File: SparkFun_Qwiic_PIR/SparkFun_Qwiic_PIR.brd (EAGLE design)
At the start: 38.1 x 25.5 mm, 39 parts, among them J1 QWIIC_RIGHT_ANGLE, J2 QWIIC_RIGHT_ANGLE, Q1 220mA/50V/3.5Ω, Q2 220mA/50V/3.5Ω, U1 PL-N823-01PL-N823-01_LENS, U2 ADS1015, U3 TPS61200

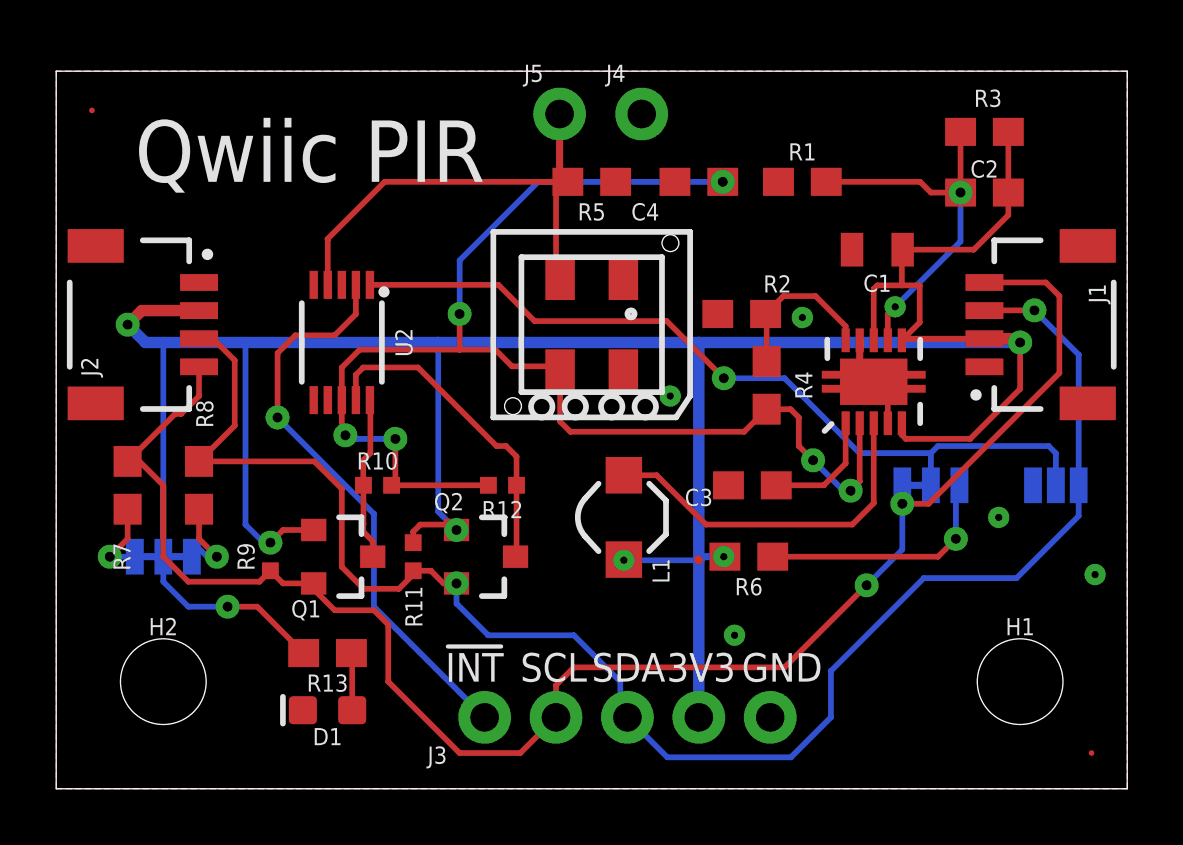
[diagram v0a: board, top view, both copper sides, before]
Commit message: Upload 15V revision with LTC3122 Boost IC
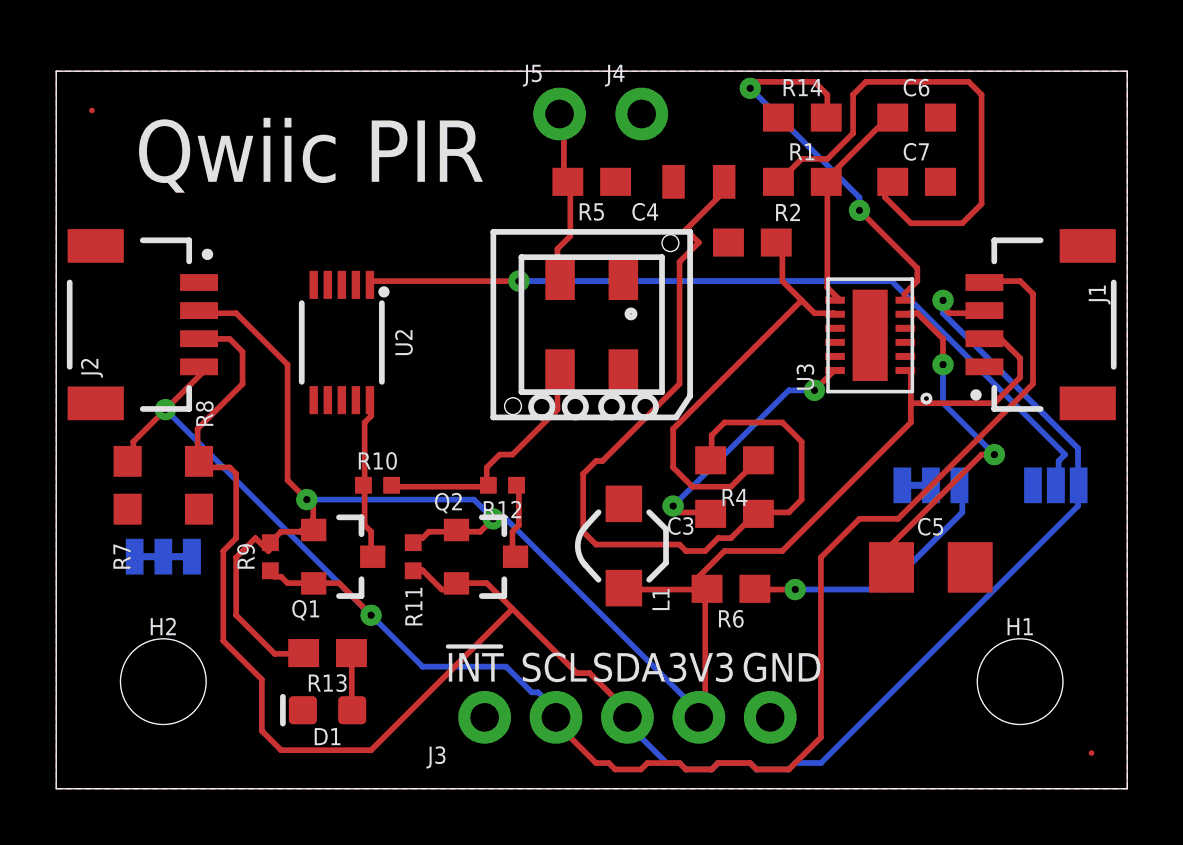
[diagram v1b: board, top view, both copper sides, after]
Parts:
- removed C1: 10uF, SparkFun-Capacitors:0805
- removed C2: 1.0uF, SparkFun-Capacitors:0603
- removed R3: 2.0M, SparkFun-Resistors:0603
- added C5: 4.7uF, SparkFun-Capacitors:1206
- added C6, C7: 1nF, SparkFun-Capacitors:0603
- added R14: 0.27, SparkFun-Resistors:0603
- C3: value 1.0uF -> 0.1uF
- C4: device SparkFun-Capacitors:0603 -> SparkFun-Capacitors:0805
- R2: value 200k -> 330
- R4: value 2.0M -> 3.3k
- U3: value TPS61200 -> LTC3122; device SparkFun-IC-Power:QFN-10_PAD -> LTC3122:LTC3122EDE#PBF
- moved R4 2.90 mm to (24.1, 11.7), turned to 180 degrees
- moved R2 2.57 mm to (24.8, 19.4)
- moved U3 1.66 mm to (29.0, 16.1), turned to 90 degrees
- moved R6 1.31 mm to (24.0, 7.11)
- moved C3 1.20 mm to (24.1, 9.78)
- moved L1 1.02 mm to (20.2, 8.64)
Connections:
- new net N$10: R2.2, R4.1, U3.P$8
- new net N$11: C6.1, R1.2, U3.P$7
- new net N$12: C7.1, R1.1
- new net N$6: C3.1, C4.1, R4.2, U3.P$11
- net 3.3V: now also U3.P$1; no longer C1.1, C2.1, R3.2, U3.5, U3.6, U3.8
- net 5V: no longer C4.1, R4.2, U3.2
- net GND: now also C5.2, C6.2, C7.2, R14.1, U3.P$10, U3.P$13, U3.P$2; no longer C1.2, C3.2, R1.1, U3.11, U3.12, U3.13, U3.14, U3.15, U3.4, U3.9
- net N$1: now also C5.1, U3.P$5; no longer L1.P$1, U3.3
- net N$3: now also L1.P$1, U3.P$3; no longer C2.2, R1.2, R3.1, U3.7
- net N$5: now also R14.2, U3.P$6; no longer R2.2, R4.1, U3.10
- net N$7: now also C3.2, U3.P$12; no longer C3.1, U3.1
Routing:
- net 3.3V: track 110.3 -> 66.4 mm, vias 7 -> 2
- net 5V: track 48.4 -> 8.96 mm, vias 6 -> 0
- net N$6: track 0.00 -> 30.5 mm
- net !INT: track 20.4 -> 0.00 mm, vias 1 -> 0
- net N$12: track 0.00 -> 18.3 mm
- net N$10: track 0.00 -> 15.5 mm
- net N$3: track 13.4 -> 0.00 mm, vias 2 -> 0
- net SDA: track 58.9 -> 71.6 mm, vias 2 -> 1
- net SOURCE: track 17.3 -> 6.34 mm
- net SDA_H: track 11.6 -> 2.71 mm
- net N$5: track 5.76 -> 14.1 mm, vias 0 -> 2
- net N$11: track 0.00 -> 8.07 mm
- net N$7: track 4.22 -> 9.19 mm, vias 0 -> 2
- net GND: track 3.36 -> 0.00 mm, vias 5 -> 0
- net N$8: track 3.00 -> 0.00 mm, vias 1 -> 0
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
